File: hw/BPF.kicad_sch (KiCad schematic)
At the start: 38 parts, among them Q401 BSS138, Q402 BSS138

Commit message: Making some progress on PIN diode bias boost converter. Page number reorg.
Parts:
- renumbered C416 to C415, C415 to C416, C418 to C417, C417 to C418
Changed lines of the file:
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@@
 		(dnp no)
 		(fields_autoplaced yes)
-		(property "Reference" "C418"
+		(property "Reference" "C417"
 			(at 194.31 68.58 90)
 			(effects
@@
 			(project "USB-SSB-txcvr"
 				(path "/8ae46c04-d01a-4756-8774-512b694bfaff/1ffb1160-1891-4fab-821d-83a4f4ddba5b/10316f80-2a51-45f2-9a70-65c0e863912d"
-					(reference "C918")
+					(reference "C917")
 					(unit 1)
 				)
 				(path "/8ae46c04-d01a-4756-8774-512b694bfaff/1ffb1160-1891-4fab-821d-83a4f4ddba5b/21fa549d-d296-4f25-917b-3728bb2bb0e6"
-					(reference "C1418")
+					(reference "C1417")
 					(unit 1)
 				)
 				(path "/8ae46c04-d01a-4756-8774-512b694bfaff/1ffb1160-1891-4fab-821d-83a4f4ddba5b/2c47d288-2a68-43b8-918a-fa74b592e58c"
-					(reference "C418")
+					(reference "C417")
 					(unit 1)
 				)
 				(path "/8ae46c04-d01a-4756-8774-512b694bfaff/1ffb1160-1891-4fab-821d-83a4f4ddba5b/30cc1af8-e416-41be-a1f5-5605b156ce2f"
-					(reference "C618")
+					(reference "C617")
 					(unit 1)
 				)
 				(path "/8ae46c04-d01a-4756-8774-512b694bfaff/1ffb1160-1891-4fab-821d-83a4f4ddba5b/3627ee59-86bf-457c-a7c4-91c03f4ee680"
-					(reference "C718")
+					(reference "C717")
 					(unit 1)
 				)
 				(path "/8ae46c04-d01a-4756-8774-512b694bfaff/1ffb1160-1891-4fab-821d-83a4f4ddba5b/3b3a2c99-e323-45ff-bfe4-1e7b718b47d8"
-					(reference "C518")
+					(reference "C517")
 					(unit 1)
 				)
 				(path "/8ae46c04-d01a-4756-8774-512b694bfaff/1ffb1160-1891-4fab-821d-83a4f4ddba5b/497540f8-78f3-4ef4-a3f6-35296d7462e0"
-					(reference "C818")
+					(reference "C817")
 					(unit 1)
 				)
 				(path "/8ae46c04-d01a-4756-8774-512b694bfaff/1ffb1160-1891-4fab-821d-83a4f4ddba5b/6ba9ed59-3ec3-4f69-a67e-b49ca49a4198"
-					(reference "C1318")
+					(reference "C1317")
 					(unit 1)
 				)
 				(path "/8ae46c04-d01a-4756-8774-512b694bfaff/1ffb1160-1891-4fab-821d-83a4f4ddba5b/90a2553f-e5d9-463d-b4a1-b25e66199157"
-					(reference "C1618")
+					(reference "C1617")
 					(unit 1)
 				)
 				(path "/8ae46c04-d01a-4756-8774-512b694bfaff/1ffb1160-1891-4fab-821d-83a4f4ddba5b/bf3aa6d8-3415-4411-a7e2-df56f25f2b45"
-					(reference "C1518")
+					(reference "C1517")
 					(unit 1)
 				)
@@
 		(on_board yes)
 		(dnp no)
-		(property "Reference" "C417"
+		(property "Reference" "C418"
 			(at 196.596 46.99 90)
 			(effects
@@
 			(project "USB-SSB-txcvr"
 				(path "/8ae46c04-d01a-4756-8774-512b694bfaff/1ffb1160-1891-4fab-821d-83a4f4ddba5b/10316f80-2a51-45f2-9a70-65c0e863912d"
-					(reference "C917")
+					(reference "C918")
 					(unit 1)
 				)
 				(path "/8ae46c04-d01a-4756-8774-512b694bfaff/1ffb1160-1891-4fab-821d-83a4f4ddba5b/21fa549d-d296-4f25-917b-3728bb2bb0e6"
-					(reference "C1417")
+					(reference "C1418")
 					(unit 1)
 				)
 				(path "/8ae46c04-d01a-4756-8774-512b694bfaff/1ffb1160-1891-4fab-821d-83a4f4ddba5b/2c47d288-2a68-43b8-918a-fa74b592e58c"
-					(reference "C417")
+					(reference "C418")
 					(unit 1)
 				)
 				(path "/8ae46c04-d01a-4756-8774-512b694bfaff/1ffb1160-1891-4fab-821d-83a4f4ddba5b/30cc1af8-e416-41be-a1f5-5605b156ce2f"
-					(reference "C617")
+					(reference "C618")
 					(unit 1)
 				)
 				(path "/8ae46c04-d01a-4756-8774-512b694bfaff/1ffb1160-1891-4fab-821d-83a4f4ddba5b/3627ee59-86bf-457c-a7c4-91c03f4ee680"
-					(reference "C717")
+					(reference "C718")
 					(unit 1)
 				)
 				(path "/8ae46c04-d01a-4756-8774-512b694bfaff/1ffb1160-1891-4fab-821d-83a4f4ddba5b/3b3a2c99-e323-45ff-bfe4-1e7b718b47d8"
-					(reference "C517")
+					(reference "C518")
 					(unit 1)
 				)
 				(path "/8ae46c04-d01a-4756-8774-512b694bfaff/1ffb1160-1891-4fab-821d-83a4f4ddba5b/497540f8-78f3-4ef4-a3f6-35296d7462e0"
-					(reference "C817")
+					(reference "C818")
 					(unit 1)
 				)
 				(path "/8ae46c04-d01a-4756-8774-512b694bfaff/1ffb1160-1891-4fab-821d-83a4f4ddba5b/6ba9ed59-3ec3-4f69-a67e-b49ca49a4198"
-					(reference "C1317")
+					(reference "C1318")
 					(unit 1)
 				)
 				(path "/8ae46c04-d01a-4756-8774-512b694bfaff/1ffb1160-1891-4fab-821d-83a4f4ddba5b/90a2553f-e5d9-463d-b4a1-b25e66199157"
-					(reference "C1617")
+					(reference "C1618")
 					(unit 1)
 				)
 				(path "/8ae46c04-d01a-4756-8774-512b694bfaff/1ffb1160-1891-4fab-821d-83a4f4ddba5b/bf3aa6d8-3415-4411-a7e2-df56f25f2b45"
-					(reference "C1517")
+					(reference "C1518")
 					(unit 1)
 				)
@@
 		(on_board yes)
 		(dnp no)
-		(property "Reference" "C415"
+		(property "Reference" "C416"
 			(at 187.706 46.736 90)
 			(effects
@@
 			(project "USB-SSB-txcvr"
 				(path "/8ae46c04-d01a-4756-8774-512b694bfaff/1ffb1160-1891-4fab-821d-83a4f4ddba5b/10316f80-2a51-45f2-9a70-65c0e863912d"
-					(reference "C915")
+					(reference "C916")
 					(unit 1)
 				)
 				(path "/8ae46c04-d01a-4756-8774-512b694bfaff/1ffb1160-1891-4fab-821d-83a4f4ddba5b/21fa549d-d296-4f25-917b-3728bb2bb0e6"
-					(reference "C1415")
+					(reference "C1416")
 					(unit 1)
 				)
 				(path "/8ae46c04-d01a-4756-8774-512b694bfaff/1ffb1160-1891-4fab-821d-83a4f4ddba5b/2c47d288-2a68-43b8-918a-fa74b592e58c"
-					(reference "C415")
+					(reference "C416")
 					(unit 1)
 				)
 				(path "/8ae46c04-d01a-4756-8774-512b694bfaff/1ffb1160-1891-4fab-821d-83a4f4ddba5b/30cc1af8-e416-41be-a1f5-5605b156ce2f"
-					(reference "C615")
+					(reference "C616")
 					(unit 1)
 				)
 				(path "/8ae46c04-d01a-4756-8774-512b694bfaff/1ffb1160-1891-4fab-821d-83a4f4ddba5b/3627ee59-86bf-457c-a7c4-91c03f4ee680"
-					(reference "C715")
+					(reference "C716")
 					(unit 1)
 				)
 				(path "/8ae46c04-d01a-4756-8774-512b694bfaff/1ffb1160-1891-4fab-821d-83a4f4ddba5b/3b3a2c99-e323-45ff-bfe4-1e7b718b47d8"
-					(reference "C515")
+					(reference "C516")
 					(unit 1)
 				)
 				(path "/8ae46c04-d01a-4756-8774-512b694bfaff/1ffb1160-1891-4fab-821d-83a4f4ddba5b/497540f8-78f3-4ef4-a3f6-35296d7462e0"
-					(reference "C815")
+					(reference "C816")
 					(unit 1)
 				)
 				(path "/8ae46c04-d01a-4756-8774-512b694bfaff/1ffb1160-1891-4fab-821d-83a4f4ddba5b/6ba9ed59-3ec3-4f69-a67e-b49ca49a4198"
-					(reference "C1315")
+					(reference "C1316")
 					(unit 1)
 				)
 				(path "/8ae46c04-d01a-4756-8774-512b694bfaff/1ffb1160-1891-4fab-821d-83a4f4ddba5b/90a2553f-e5d9-463d-b4a1-b25e66199157"
-					(reference "C1615")
+					(reference "C1616")
 					(unit 1)
 				)
 				(path "/8ae46c04-d01a-4756-8774-512b694bfaff/1ffb1160-1891-4fab-821d-83a4f4ddba5b/bf3aa6d8-3415-4411-a7e2-df56f25f2b45"
-					(reference "C1515")
+					(reference "C1516")
 					(unit 1)
 				)
@@
 		(on_board yes)
 		(dnp no)
-		(property "Reference" "C416"
+		(property "Reference" "C415"
 			(at 194.056 84.328 0)
 			(effects
@@
 			(project "USB-SSB-txcvr"
 				(path "/8ae46c04-d01a-4756-8774-512b694bfaff/1ffb1160-1891-4fab-821d-83a4f4ddba5b/10316f80-2a51-45f2-9a70-65c0e863912d"
-					(reference "C916")
+					(reference "C915")
 					(unit 1)
 				)
 				(path "/8ae46c04-d01a-4756-8774-512b694bfaff/1ffb1160-1891-4fab-821d-83a4f4ddba5b/21fa549d-d296-4f25-917b-3728bb2bb0e6"
-					(reference "C1416")
+					(reference "C1415")
 					(unit 1)
 				)
 				(path "/8ae46c04-d01a-4756-8774-512b694bfaff/1ffb1160-1891-4fab-821d-83a4f4ddba5b/2c47d288-2a68-43b8-918a-fa74b592e58c"
-					(reference "C416")
+					(reference "C415")
 					(unit 1)
 				)
 				(path "/8ae46c04-d01a-4756-8774-512b694bfaff/1ffb1160-1891-4fab-821d-83a4f4ddba5b/30cc1af8-e416-41be-a1f5-5605b156ce2f"
-					(reference "C616")
+					(reference "C615")
 					(unit 1)
 				)
 				(path "/8ae46c04-d01a-4756-8774-512b694bfaff/1ffb1160-1891-4fab-821d-83a4f4ddba5b/3627ee59-86bf-457c-a7c4-91c03f4ee680"
-					(reference "C716")
+					(reference "C715")
 					(unit 1)
 				)
 				(path "/8ae46c04-d01a-4756-8774-512b694bfaff/1ffb1160-1891-4fab-821d-83a4f4ddba5b/3b3a2c99-e323-45ff-bfe4-1e7b718b47d8"
-					(reference "C516")
+					(reference "C515")
 					(unit 1)
 				)
 				(path "/8ae46c04-d01a-4756-8774-512b694bfaff/1ffb1160-1891-4fab-821d-83a4f4ddba5b/497540f8-78f3-4ef4-a3f6-35296d7462e0"
-					(reference "C816")
+					(reference "C815")
 					(unit 1)
 				)
 				(path "/8ae46c04-d01a-4756-8774-512b694bfaff/1ffb1160-1891-4fab-821d-83a4f4ddba5b/6ba9ed59-3ec3-4f69-a67e-b49ca49a4198"
-					(reference "C1316")
+					(reference "C1315")
 					(unit 1)
 				)
 				(path "/8ae46c04-d01a-4756-8774-512b694bfaff/1ffb1160-1891-4fab-821d-83a4f4ddba5b/90a2553f-e5d9-463d-b4a1-b25e66199157"
-					(reference "C1616")
+					(reference "C1615")
 					(unit 1)
 				)
 				(path "/8ae46c04-d01a-4756-8774-512b694bfaff/1ffb1160-1891-4fab-821d-83a4f4ddba5b/bf3aa6d8-3415-4411-a7e2-df56f25f2b45"
-					(reference "C1516")
+					(reference "C1515")
 					(unit 1)
 				)

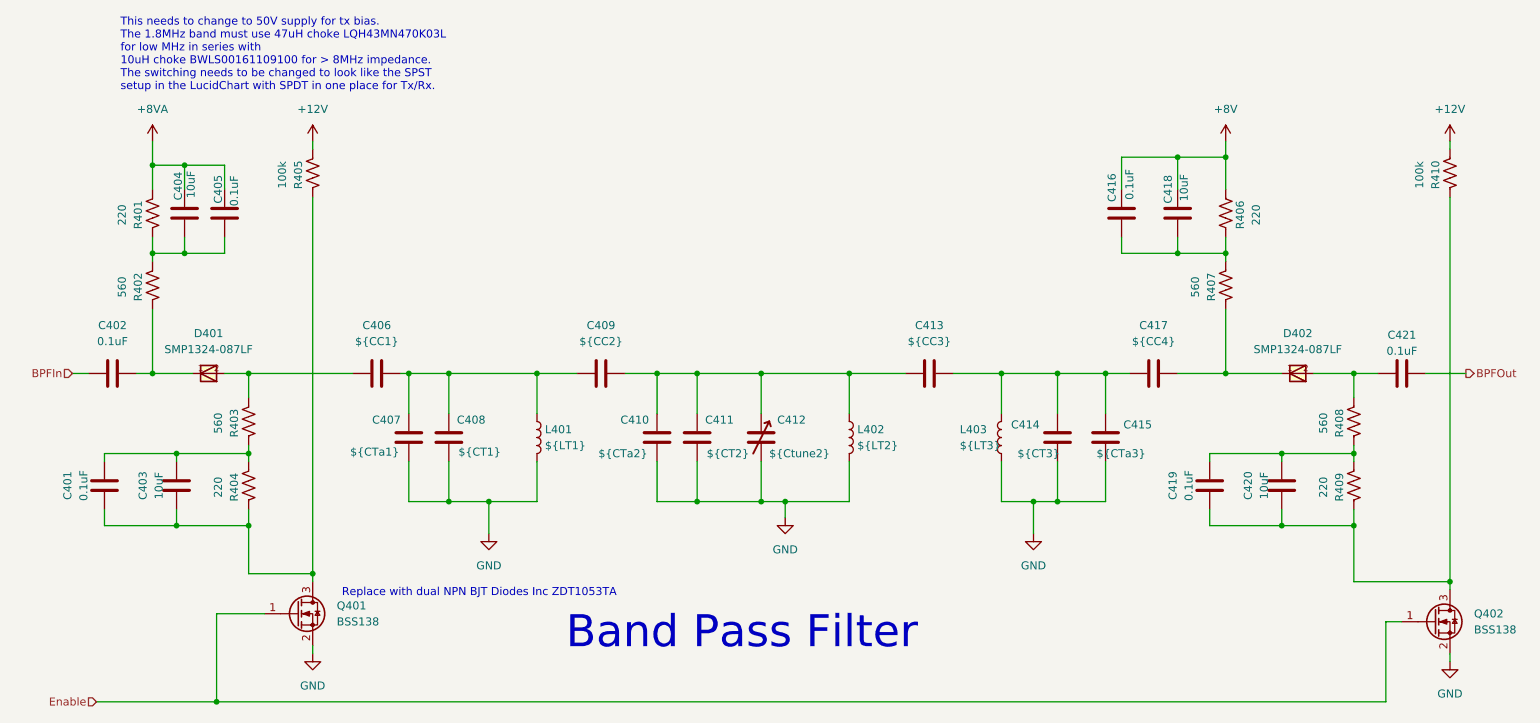
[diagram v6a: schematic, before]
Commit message: Tx LPF and its selection is pretty much done. Fix some OCD. Start to describe the design and construction.
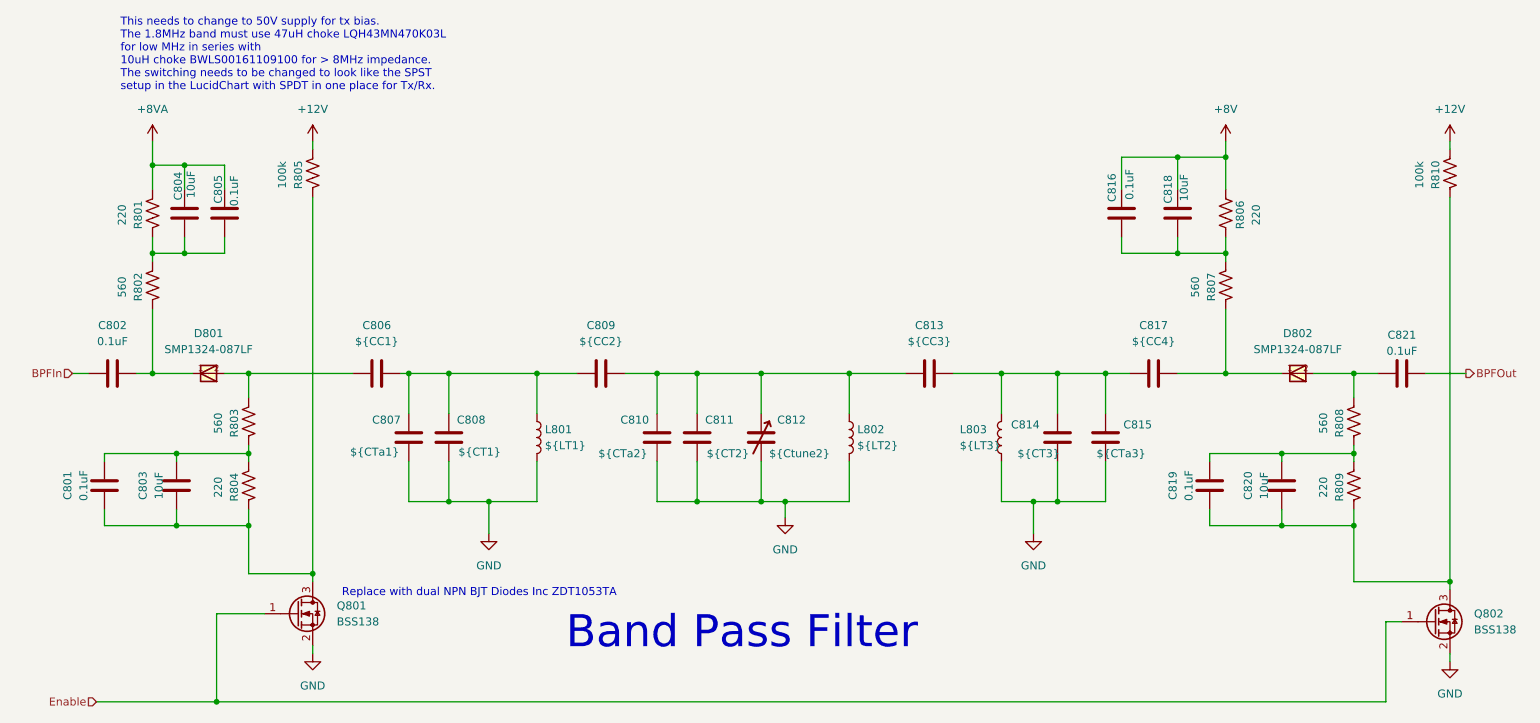
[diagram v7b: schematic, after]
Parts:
- renumbered C401 to C801, C402 to C802, C403 to C803, C404 to C804, C405 to C805, C406 to C806, C407 to C807, C408 to C808, C409 to C809, C410 to C810, C411 to C811, C412 to C812, C413 to C813, C414 to C814, C415 to C815, C416 to C816, C417 to C817, C418 to C818, C419 to C819, C420 to C820, C421 to C821, D401 to D801, D402 to D802, L401 to L801, L402 to L802, L403 to L803, Q401 to Q801, Q402 to Q802, R401 to R801, R402 to R802, R403 to R803, R404 to R804, R405 to R805, R406 to R806, R407 to R807, R408 to R808, R409 to R809, R410 to R810

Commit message: Checkpoint
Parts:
- removed C801, C802, C805, C816, C819, C821: 0.1uF, symbol Device:C
- removed C803, C804, C818, C820: 10uF, symbol Device:C
- removed D801, D802: SMP1324-087LF, SMP1324-087LF:QFN2, symbol SMP1324-087LF:SMP1324-087LF
- removed Q801, Q802: BSS138, Package_TO_SOT_SMD:SOT-23, symbol Transistor_FET:BSS138
- removed R801, R804, R806, R809: 220, symbol Device:R_US
- removed R802, R803, R807, R808: 560, symbol Device:R_US
- removed R805, R810: 100k, symbol Device:R_US
- added C1501, C1502: 0.1uF, symbol Device:C
- added IC1501: AS169-73LF, SOT95P270X145-6N, symbol AS169-73LF:AS169-73LF
- added IC1502: MC74HC1G04DFT2G-Q, MC74HC1G04DFT2GQ, symbol MC74HC1G04DFT2G-Q:MC74HC1G04DFT2G-Q
- renumbered C806 to C1503, C807 to C1504, C808 to C1505, C809 to C1506, C810 to C1507, C811 to C1508, C812 to C1509, C813 to C1510, C814 to C1511, C815 to C1512, C817 to C1513, L801 to L1501, L802 to L1502, L803 to L1503
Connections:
- net BPFIn: now also C1501.1
- net Enable: now also IC1501.4 (V1), IC1502.2 (A)
- net GND: now also C1502.2, IC1501.2 (GND), IC1501.3 (J2), IC1502.3 (GND)
- net at C1503.1: now also IC1501.5 (J1)
- net BPFout: now reaches C1513.2
- new net: C1501.2, IC1501.1 (J3)
- new net +3.3V: C1502.1, IC1502.5 (VCC)
- new net BPFdisable: IC1501.6 (V2), IC1502.4 (Y)
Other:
- note removed: "Replace with dual NPN BJT Diodes Inc ZDT1053TA"
- note removed: "This needs to change to 50V supply for tx bias. The 1.8MHz band must use 47uH choke LQH43MN470K03L for low MHz in series with 10uH choke BWLS00161109100 for > 8MHz impedance. The switching needs to be changed to look like the SPST setup in the LucidChart with SPDT in one place for Tx/Rx."
- moved on the sheet: C1503, C1504, C1505, C1506, C1507, C1508, C1509, C1510, C1511, C1512, C1513, L1501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
